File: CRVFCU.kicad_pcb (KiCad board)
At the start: 4 copper layers, 50 x 100 mm, 161 parts, among them J1 TagConnect_TC2030, J2 Conn_01x02, J3 USB_C_Receptacle_USB2.0_16P, J4 Micro_SD_Card_Det2, J5 Conn_01x02, Q3 DMG2301L, Q4 BC818, Q5 DMG2301L, Q6 DMG2301L, U1 MS5611-01BA, U10 W25Q128JVS, U11 EClamp2515K, U12 ESDALC6V1W5, U13 USBLC6-2SC6, U14 USBLC6-2SC6, U15 MAX17049, U16 SI7232DN-T1, U17 SN74LV1T34DCK, U18 AP63205WU, U2 STM32H747IITx, U3 LIS2MDL, U4 ICM-45686, U5 FXMA108, U7 AP1117-33, U8 SI7232DN-T1, U9 USBLC6-4SC6, Y1 ECS-.327-6-34QCS-TR, Y2 ECS-250-10-33B-CKY-TR3, Y3 32.768khz

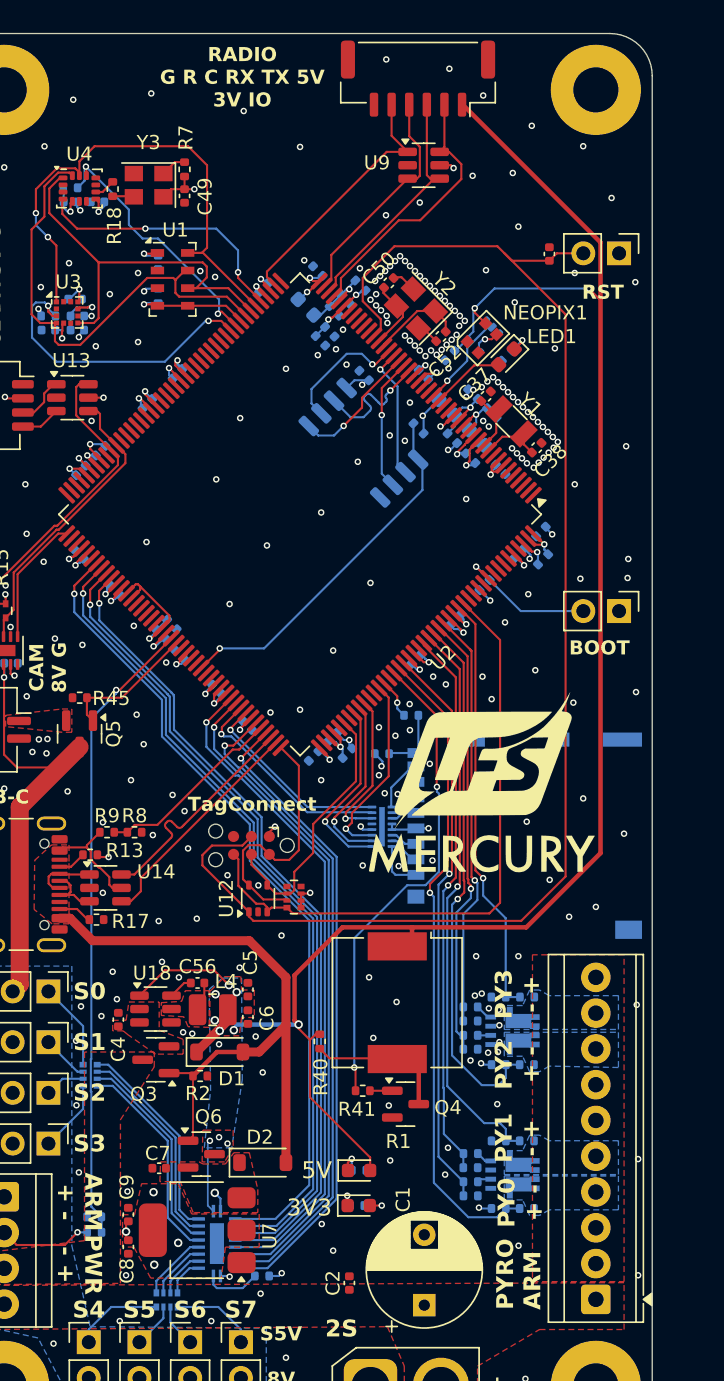
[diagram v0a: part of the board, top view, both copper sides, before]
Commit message: added protection diode for buck and changed routing for thermal considerations
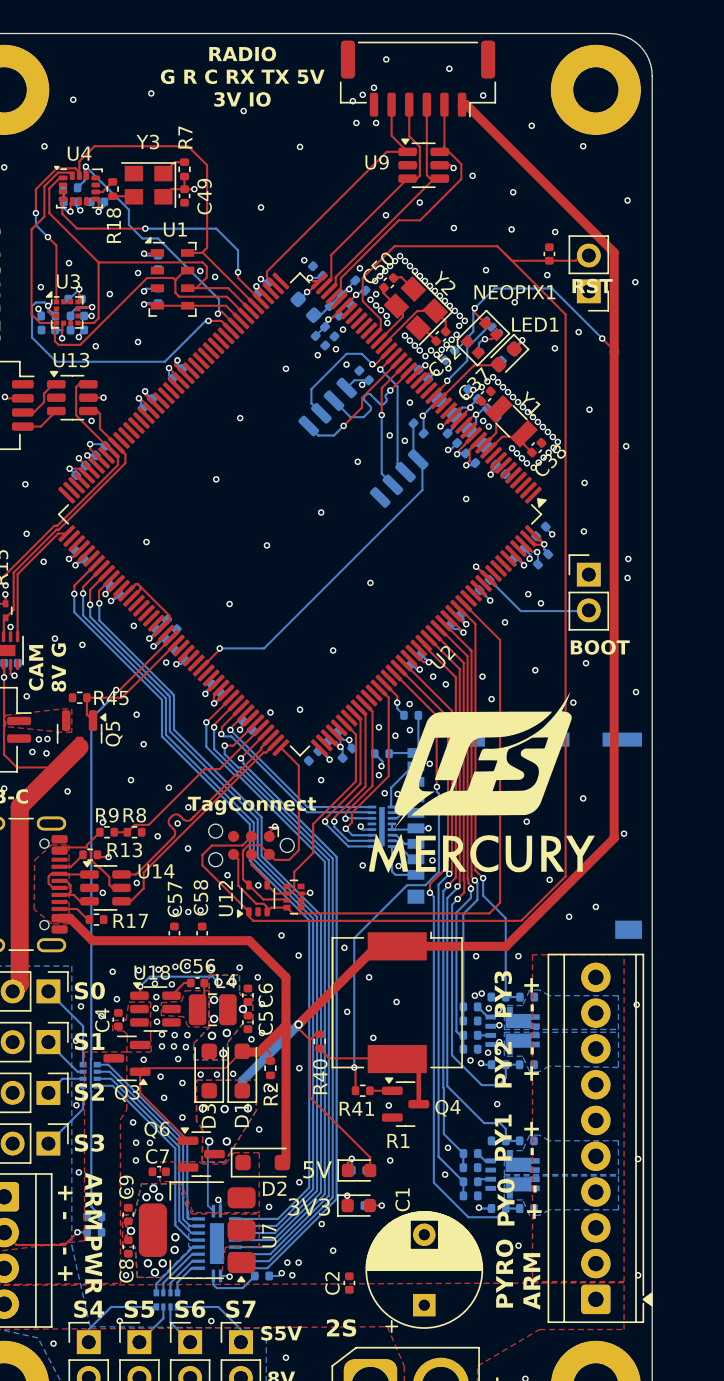
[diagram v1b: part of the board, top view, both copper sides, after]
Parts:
- added C57: 10uF, Capacitor_SMD:C_0402_1005Metric, F.Cu at (56.1, 83.9)
- added C58: 10uF, Capacitor_SMD:C_0402_1005Metric, F.Cu at (58.0, 83.9)
- added D3: SMD26PL-TP, Diode_SMD:D_SOD-123F, F.Cu at (58.5, 93.7)
- D1, D2: value MBR0540 -> SMD26PL-TP; footprint Diode_SMD:D_SOD-123 -> Diode_SMD:D_SOD-123F
- moved R2 5.02 mm to (62.9, 93.5), turned to -90 degrees
- moved J2 3.45 mm to (85.5, 38.3), turned to 180 degrees
- moved J5 3.37 mm to (85.5, 58.4), turned to 0 degrees
- moved C5 2.33 mm to (61.3, 90.2), turned to -90 degrees
- moved D1 2.09 mm to (60.9, 93.7), turned to 90 degrees
- moved Q3 2.05 mm to (52.7, 92.8)
- moved C6 1.55 mm to (61.3, 88.3), turned to 90 degrees
- moved C7 0.25 mm to (55.0, 100.8)
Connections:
- C5 pad 1: +5V -> Net-(D3-A)
- C6 pad 1: +5V -> Net-(D3-A)
- L4 pad 2: +5V -> Net-(D3-A)
- U18 pad 1: +5V -> Net-(D3-A)
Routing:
- net +5V: track 137.8 -> 127.7 mm, vias 12 -> 8
- net Net-(D3-A): track 0.00 -> 8.32 mm, vias 0 -> 9
- net VBUS: track 53.8 -> 58.3 mm
- net GND: track 43.2 -> 44.2 mm, vias 268 -> 319
- net +3V3: track 89.6 -> 89.5 mm, vias 48 -> 53
- added copper zone on B.Cu, net +3V3
- added copper zone on B.Cu, net Net-(D3-A)
- added copper zone on F.Cu, net Net-(D3-A)

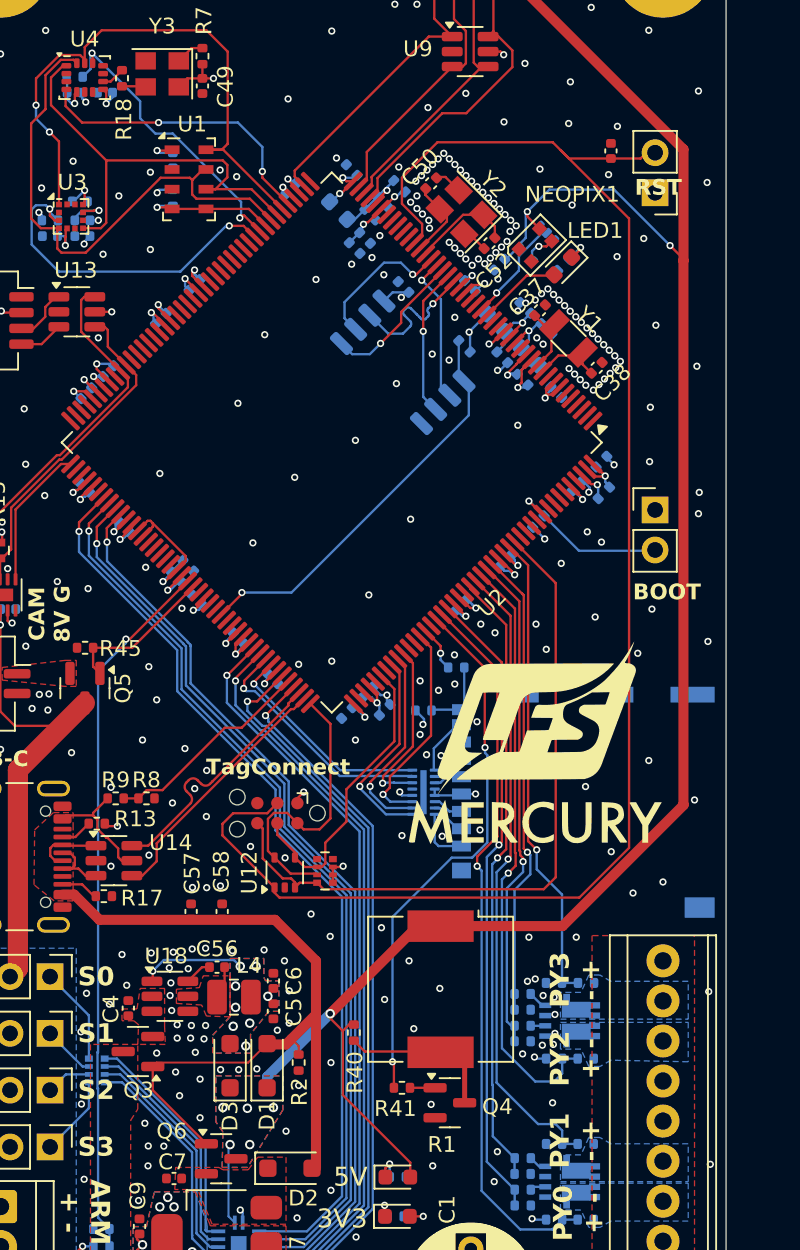
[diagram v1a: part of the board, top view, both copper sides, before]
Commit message: changed to higher current mosfet for power supply switching and fixed silkscreens
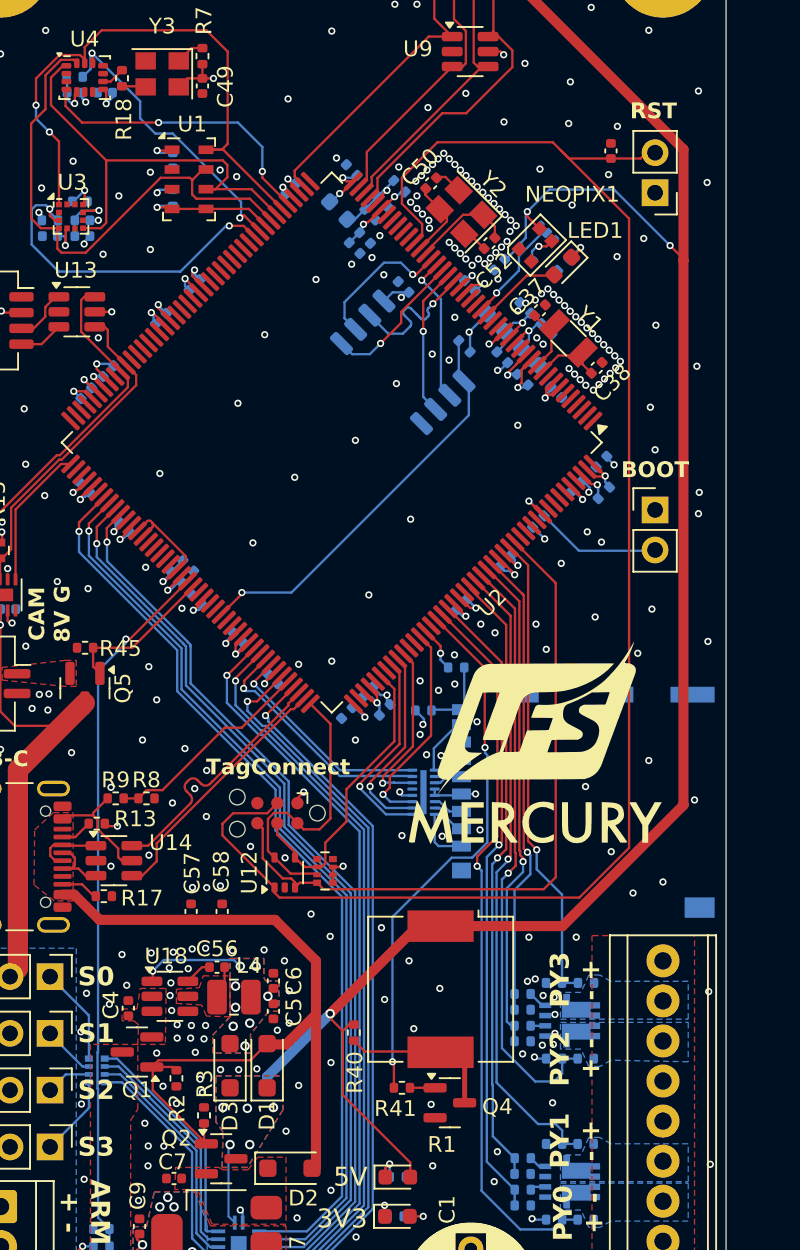
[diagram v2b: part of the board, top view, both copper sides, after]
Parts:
- removed Q3, Q6: DMG2301L, Package_TO_SOT_SMD:SOT-23
- added Q1: AO3401A, Package_TO_SOT_SMD:SOT-23, F.Cu at (52.7, 92.8)
- added Q2: AO3401A, Package_TO_SOT_SMD:SOT-23, F.Cu at (58.0, 99.5)
- added R3: 10k, Resistor_SMD:R_0402_1005Metric, F.Cu at (56.9, 96.8)
- U7: value AP1117-33 -> LDL1117S33R
- moved R2 7.81 mm to (55.1, 94.5)
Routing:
- net VBUS: track 58.3 -> 60.2 mm

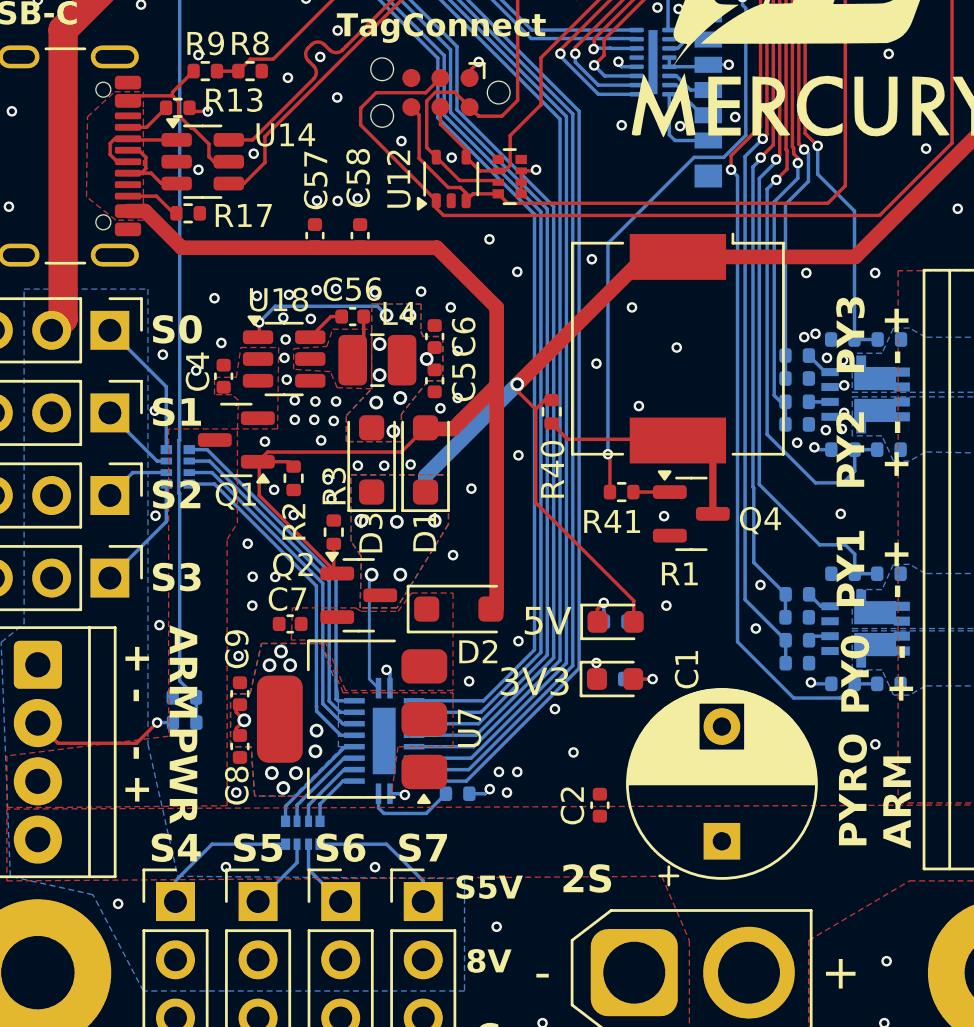
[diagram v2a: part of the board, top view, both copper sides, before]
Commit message: simplified power delivery
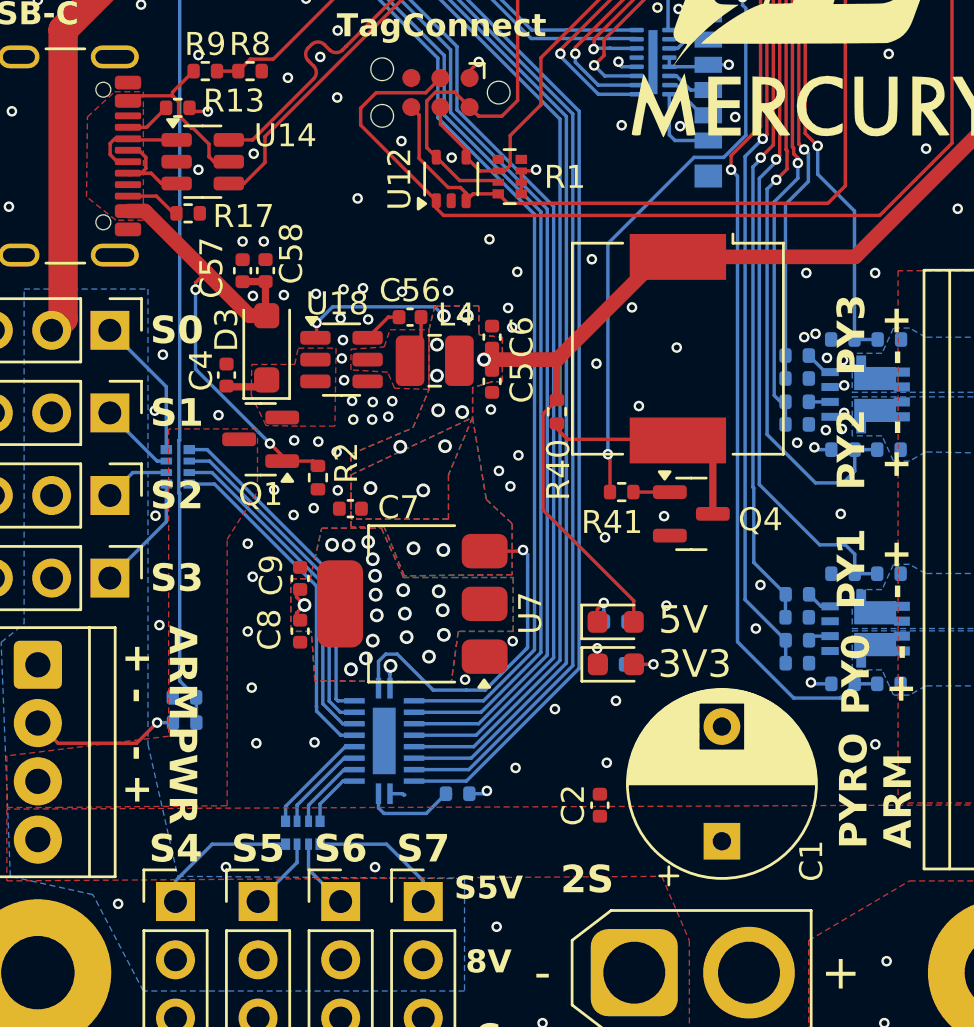
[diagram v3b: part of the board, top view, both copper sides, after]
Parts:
- removed D1, D2: SMD26PL-TP, Diode_SMD:D_SOD-123F
- removed Q2: AO3401A, Package_TO_SOT_SMD:SOT-23
- removed R3: 10k, Resistor_SMD:R_0402_1005Metric
- moved D3 6.69 mm to (54.0, 88.8)
- moved C8 5.67 mm to (55.4, 101.1)
- moved C9 5.67 mm to (55.4, 98.8)
- moved U7 5.67 mm to (60.3, 99.9)
- moved C7 5.67 mm to (57.6, 95.8)
- moved C58 4.40 mm to (53.9, 85.4)
- moved C57 3.51 mm to (52.9, 85.4)
- moved C5 2.50 mm to (63.8, 90.2)
- moved C56 2.50 mm to (60.2, 87.4)
- moved C6 2.50 mm to (63.8, 88.3)
- moved L4 2.50 mm to (61.3, 89.3)
- moved U18 2.50 mm to (57.2, 89.3)
- moved R2 1.06 mm to (56.2, 94.4)
- moved Q1 1.06 mm to (53.7, 92.8)
- moved 3V3_PWR1 0.64 mm to (69.2, 102.6)
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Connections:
- C4 pad 1: Net-(Q1-S) -> Net-(D3-K)
- C5 pad 1: Net-(D3-A) -> +5V
- C6 pad 1: Net-(D3-A) -> +5V
- C7 pad 1: Net-(D2-K) -> +5V
- D3 pad 1: +5V -> Net-(D3-K)
- D3 pad 2: Net-(D3-A) -> VBUS
- L4 pad 2: Net-(D3-A) -> +5V
- Q1 pad 2: Net-(Q1-S) -> Net-(D3-K)
- U18 pad 1: Net-(D3-A) -> +5V
- U18 pad 2: Net-(Q1-S) -> Net-(D3-K)
- U18 pad 3: Net-(Q1-S) -> Net-(D3-K)
- U7 pad 3: Net-(D2-K) -> +5V
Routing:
- net VBUS: track 60.2 -> 30.3 mm, vias 0 -> 2
- net +5V: track 127.7 -> 141.9 mm, vias 8 -> 17
- net Net-(D3-A): track 8.32 -> 0.00 mm, vias 9 -> 0
- net Net-(D3-K): track 0.00 -> 1.87 mm
- net Net-(3V3_PWR1-K): track 1.54 -> 0.86 mm
- net +3V3: track 89.5 -> 89.6 mm, vias 53 -> 62
- net GND: vias 319 -> 314
- added copper zone on F.Cu, net Net-(D3-K)
- removed copper zone on F.Cu, net Net-(D2-K)
- removed copper zone on B.Cu, net Net-(D3-A)
- removed copper zone on F.Cu, net Net-(D3-A)
- removed copper zone on F.Cu, net Net-(Q1-S)

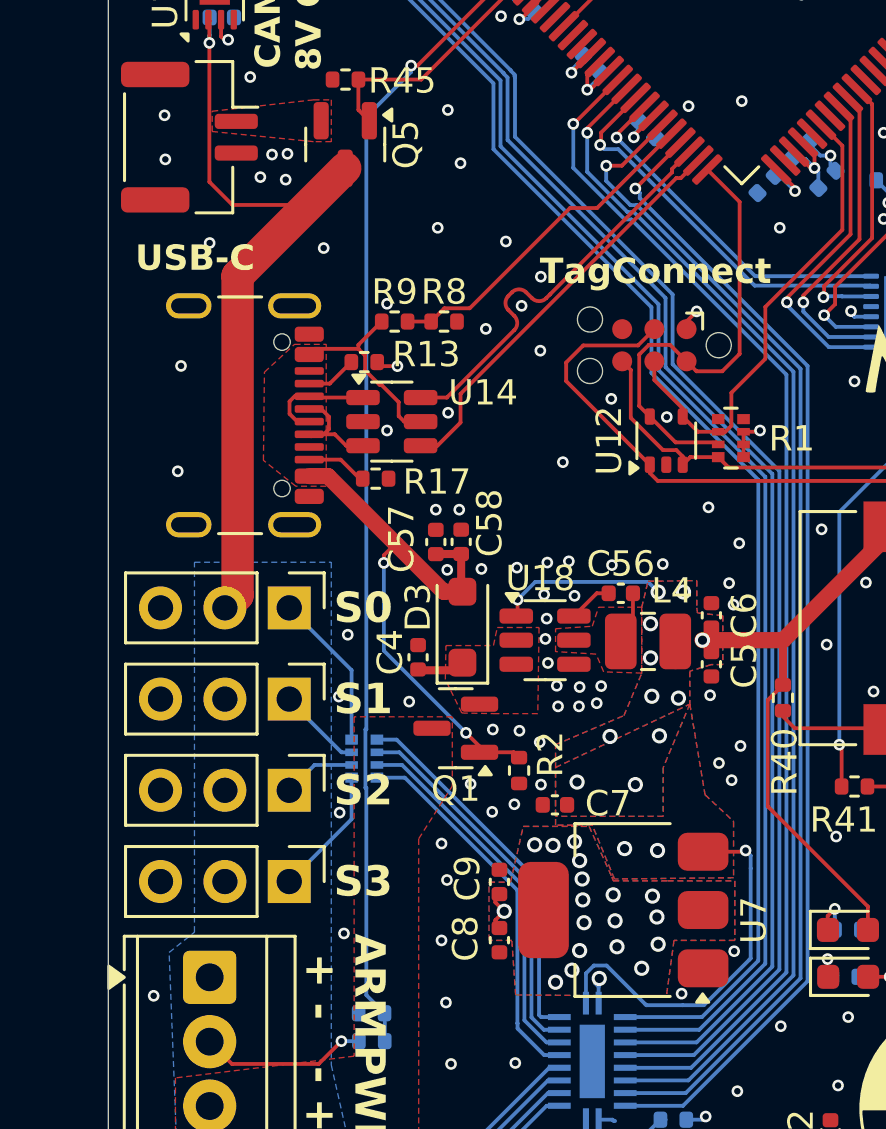
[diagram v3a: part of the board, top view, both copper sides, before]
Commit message: adjusted usbc port and 5v pour dimensions
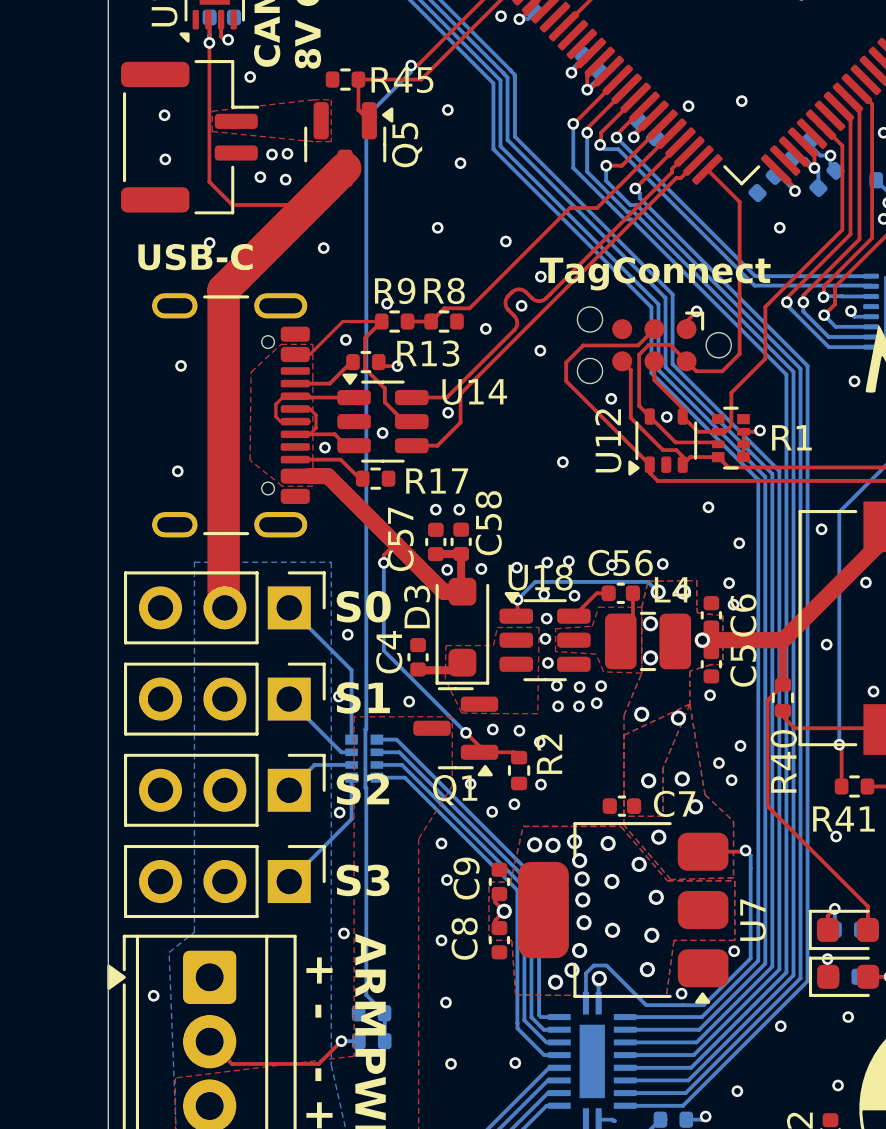
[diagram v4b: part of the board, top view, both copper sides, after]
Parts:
- moved C7 2.65 mm to (60.3, 95.8)
- moved J3 0.55 mm to (43.7, 80.4)
- moved U14 0.35 mm to (50.8, 80.7)
- moved R13 0.06 mm to (50.2, 78.3)
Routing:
- net VBUS: track 30.3 -> 31.5 mm
- net Net-(J3-D--PadA7): track 4.40 -> 5.42 mm
- net GND: vias 314 -> 316
- net +5V: vias 17 -> 15
